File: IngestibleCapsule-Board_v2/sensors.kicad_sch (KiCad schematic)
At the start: 7 parts, among them U2 MLX90640, U3 ADXL343

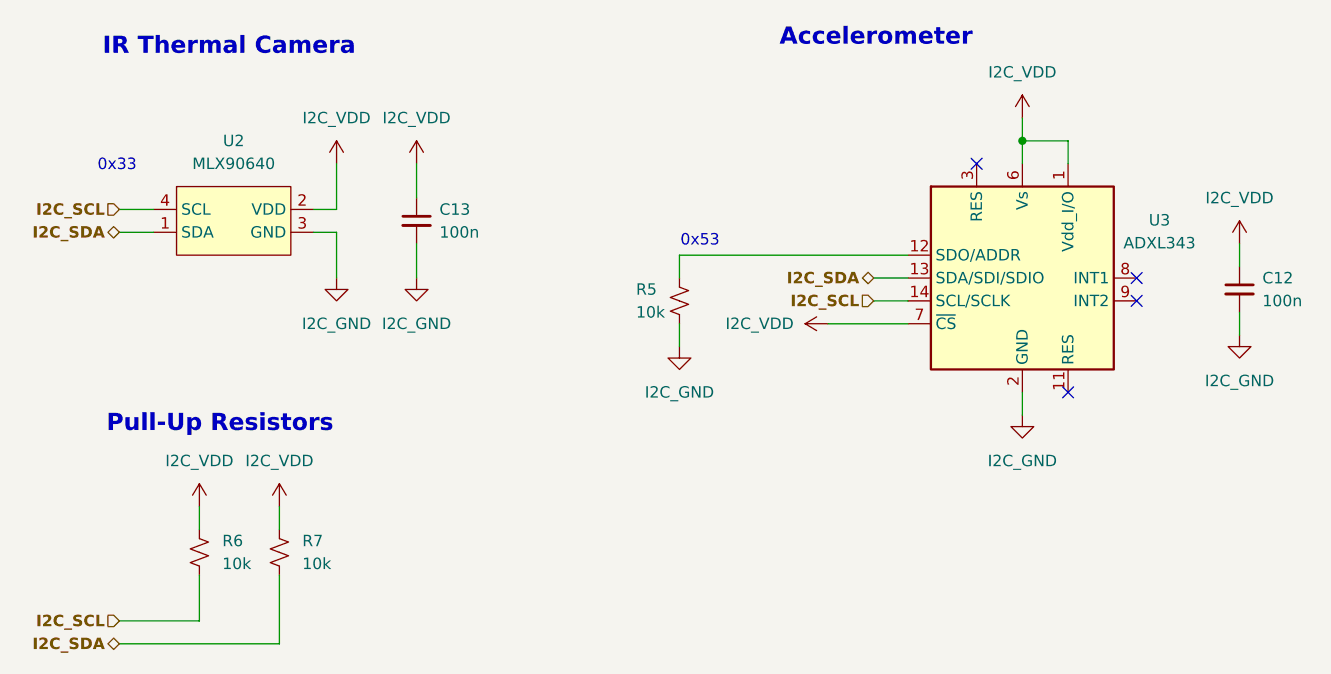
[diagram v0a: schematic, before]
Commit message: full v2 implementation, has 5 circles connected by mousebites
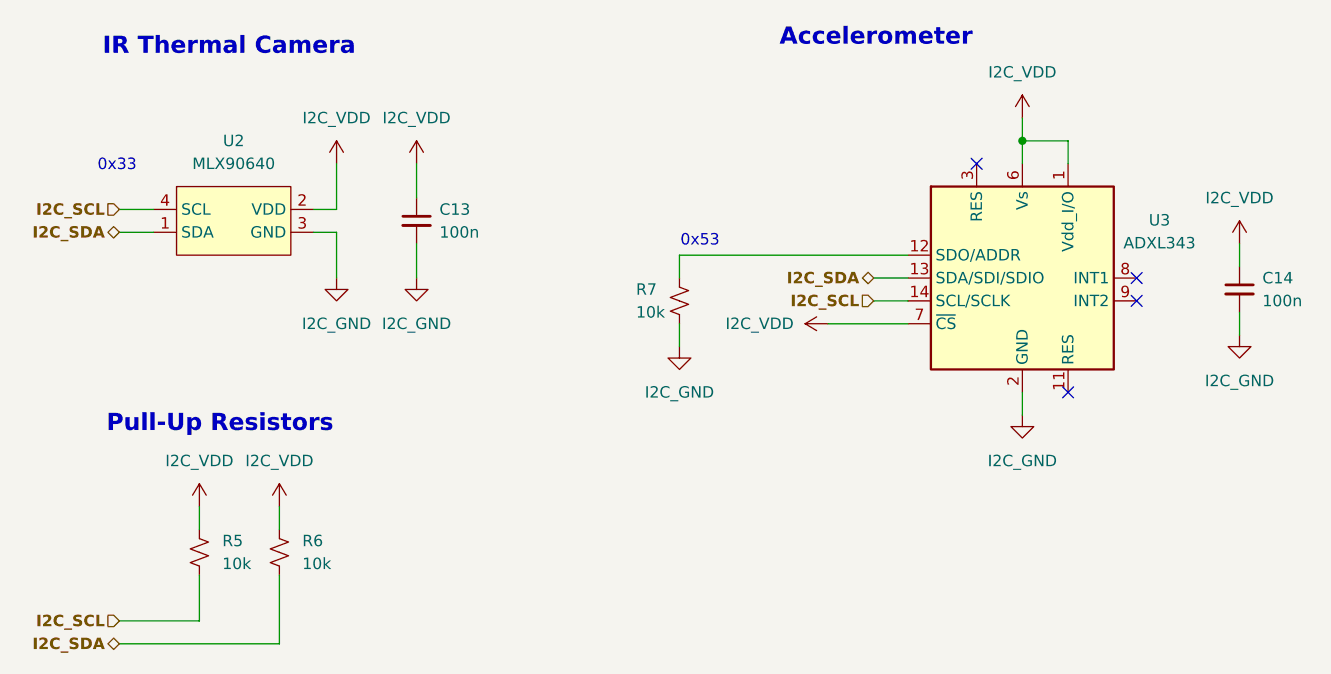
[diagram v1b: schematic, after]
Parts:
- renumbered C12 to C14, R6 to R5, R7 to R6, R5 to R7
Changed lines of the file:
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@@
 		(on_board yes)
 		(dnp no)
-		(property "Reference" "R5"
+		(property "Reference" "R7"
 			(at 119.634 106.68 0)
 			(effects
@@
 			(project ""
 				(path "/c8668ce4-f244-4f6b-86d5-e45f0742e988/db65d08b-836e-4eb4-bfdc-afb5cab3bc08"
-					(reference "R5")
+					(reference "R7")
 					(unit 1)
 				)
@@
 		(dnp no)
 		(fields_autoplaced yes)
-		(property "Reference" "#PWR059"
+		(property "Reference" "#PWR035"
 			(at 71.12 134.62 0)
 			(effects
@@
 			(project "IngestibleCapsule-Board"
 				(path "/c8668ce4-f244-4f6b-86d5-e45f0742e988/db65d08b-836e-4eb4-bfdc-afb5cab3bc08"
-					(reference "#PWR059")
+					(reference "#PWR035")
 					(unit 1)
 				)
@@
 		(dnp no)
 		(fields_autoplaced yes)
-		(property "Reference" "#PWR018"
+		(property "Reference" "#PWR038"
 			(at 86.36 111.76 0)
 			(effects
@@
 			(project ""
 				(path "/c8668ce4-f244-4f6b-86d5-e45f0742e988/db65d08b-836e-4eb4-bfdc-afb5cab3bc08"
-					(reference "#PWR018")
+					(reference "#PWR038")
 					(unit 1)
 				)
@@
 		(dnp no)
 		(fields_autoplaced yes)
-		(property "Reference" "C12"
+		(property "Reference" "C14"
 			(at 189.23 105.4162 0)
 			(effects
@@
 			(project ""
 				(path "/c8668ce4-f244-4f6b-86d5-e45f0742e988/db65d08b-836e-4eb4-bfdc-afb5cab3bc08"
-					(reference "C12")
+					(reference "C14")
 					(unit 1)
 				)
@@
 		(dnp no)
 		(fields_autoplaced yes)
-		(property "Reference" "R6"
+		(property "Reference" "R5"
 			(at 73.66 134.6199 0)
 			(effects
@@
 			(project "IngestibleCapsule-Board"
 				(path "/c8668ce4-f244-4f6b-86d5-e45f0742e988/db65d08b-836e-4eb4-bfdc-afb5cab3bc08"
-					(reference "R6")
+					(reference "R5")
 					(unit 1)
 				)
@@
 		(dnp no)
 		(fields_autoplaced yes)
-		(property "Reference" "#PWR055"
+		(property "Reference" "#PWR039"
 			(at 95.25 96.52 0)
 			(effects
@@
 			(project "IngestibleCapsule-Board"
 				(path "/c8668ce4-f244-4f6b-86d5-e45f0742e988/db65d08b-836e-4eb4-bfdc-afb5cab3bc08"
-					(reference "#PWR055")
+					(reference "#PWR039")
 					(unit 1)
 				)
@@
 		(dnp no)
 		(fields_autoplaced yes)
-		(property "Reference" "#PWR054"
+		(property "Reference" "#PWR037"
 			(at 86.36 96.52 0)
 			(effects
@@
 			(project ""
 				(path "/c8668ce4-f244-4f6b-86d5-e45f0742e988/db65d08b-836e-4eb4-bfdc-afb5cab3bc08"
-					(reference "#PWR054")
+					(reference "#PWR037")
 					(unit 1)
 				)
@@
 		(dnp no)
 		(fields_autoplaced yes)
-		(property "Reference" "#PWR020"
+		(property "Reference" "#PWR046"
 			(at 186.69 118.11 0)
 			(effects
@@
 			(project "IngestibleCapsule-Board"
 				(path "/c8668ce4-f244-4f6b-86d5-e45f0742e988/db65d08b-836e-4eb4-bfdc-afb5cab3bc08"
-					(reference "#PWR020")
+					(reference "#PWR046")
 					(unit 1)
 				)
@@
 		(dnp no)
 		(fields_autoplaced yes)
-		(property "Reference" "#PWR022"
+		(property "Reference" "#PWR044"
 			(at 162.56 127 0)
 			(effects
@@
 			(project "IngestibleCapsule-Board"
 				(path "/c8668ce4-f244-4f6b-86d5-e45f0742e988/db65d08b-836e-4eb4-bfdc-afb5cab3bc08"
-					(reference "#PWR022")
+					(reference "#PWR044")
 					(unit 1)
 				)
@@
 		(dnp no)
 		(fields_autoplaced yes)
-		(property "Reference" "#PWR019"
+		(property "Reference" "#PWR040"
 			(at 95.25 111.76 0)
 			(effects
@@
 			(project "IngestibleCapsule-Board"
 				(path "/c8668ce4-f244-4f6b-86d5-e45f0742e988/db65d08b-836e-4eb4-bfdc-afb5cab3bc08"
-					(reference "#PWR019")
+					(reference "#PWR040")
 					(unit 1)
 				)
@@
 		(dnp no)
 		(fields_autoplaced yes)
-		(property "Reference" "#PWR057"
+		(property "Reference" "#PWR045"
 			(at 186.69 105.41 0)
 			(effects
@@
 			(project "IngestibleCapsule-Board"
 				(path "/c8668ce4-f244-4f6b-86d5-e45f0742e988/db65d08b-836e-4eb4-bfdc-afb5cab3bc08"
-					(reference "#PWR057")
+					(reference "#PWR045")
 					(unit 1)
 				)
@@
 		(dnp no)
 		(fields_autoplaced yes)
-		(property "Reference" "#PWR021"
+		(property "Reference" "#PWR041"
 			(at 124.46 119.38 0)
 			(effects
@@
 			(project "IngestibleCapsule-Board"
 				(path "/c8668ce4-f244-4f6b-86d5-e45f0742e988/db65d08b-836e-4eb4-bfdc-afb5cab3bc08"
-					(reference "#PWR021")
+					(reference "#PWR041")
 					(unit 1)
 				)
@@
 		(dnp no)
 		(fields_autoplaced yes)
-		(property "Reference" "#PWR058"
+		(property "Reference" "#PWR042"
 			(at 144.78 110.49 0)
 			(effects
@@
 			(project "IngestibleCapsule-Board"
 				(path "/c8668ce4-f244-4f6b-86d5-e45f0742e988/db65d08b-836e-4eb4-bfdc-afb5cab3bc08"
-					(reference "#PWR058")
+					(reference "#PWR042")
 					(unit 1)
 				)
@@
 		(dnp no)
 		(fields_autoplaced yes)
-		(property "Reference" "#PWR056"
+		(property "Reference" "#PWR043"
 			(at 162.56 91.44 0)
 			(effects
@@
 			(project "IngestibleCapsule-Board"
 				(path "/c8668ce4-f244-4f6b-86d5-e45f0742e988/db65d08b-836e-4eb4-bfdc-afb5cab3bc08"
-					(reference "#PWR056")
+					(reference "#PWR043")
 					(unit 1)
 				)
@@
 		(dnp no)
 		(fields_autoplaced yes)
-		(property "Reference" "R7"
+		(property "Reference" "R6"
 			(at 82.55 134.6199 0)
 			(effects
@@
 			(project "IngestibleCapsule-Board"
 				(path "/c8668ce4-f244-4f6b-86d5-e45f0742e988/db65d08b-836e-4eb4-bfdc-afb5cab3bc08"
-					(reference "R7")
+					(reference "R6")
 					(unit 1)
 				)
@@
 		(dnp no)
 		(fields_autoplaced yes)
-		(property "Reference" "#PWR060"
+		(property "Reference" "#PWR036"
 			(at 80.01 134.62 0)
 			(effects
@@
 			(project "IngestibleCapsule-Board"
 				(path "/c8668ce4-f244-4f6b-86d5-e45f0742e988/db65d08b-836e-4eb4-bfdc-afb5cab3bc08"
-					(reference "#PWR060")
-					(unit 1)
-				)
+					(reference "#PWR036")
+					(unit 1)
+				)
